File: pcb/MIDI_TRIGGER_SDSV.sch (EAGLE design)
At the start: 20 parts, among them IC1 AT90S2313P, IC7 7805TV, J1 DCJ0202

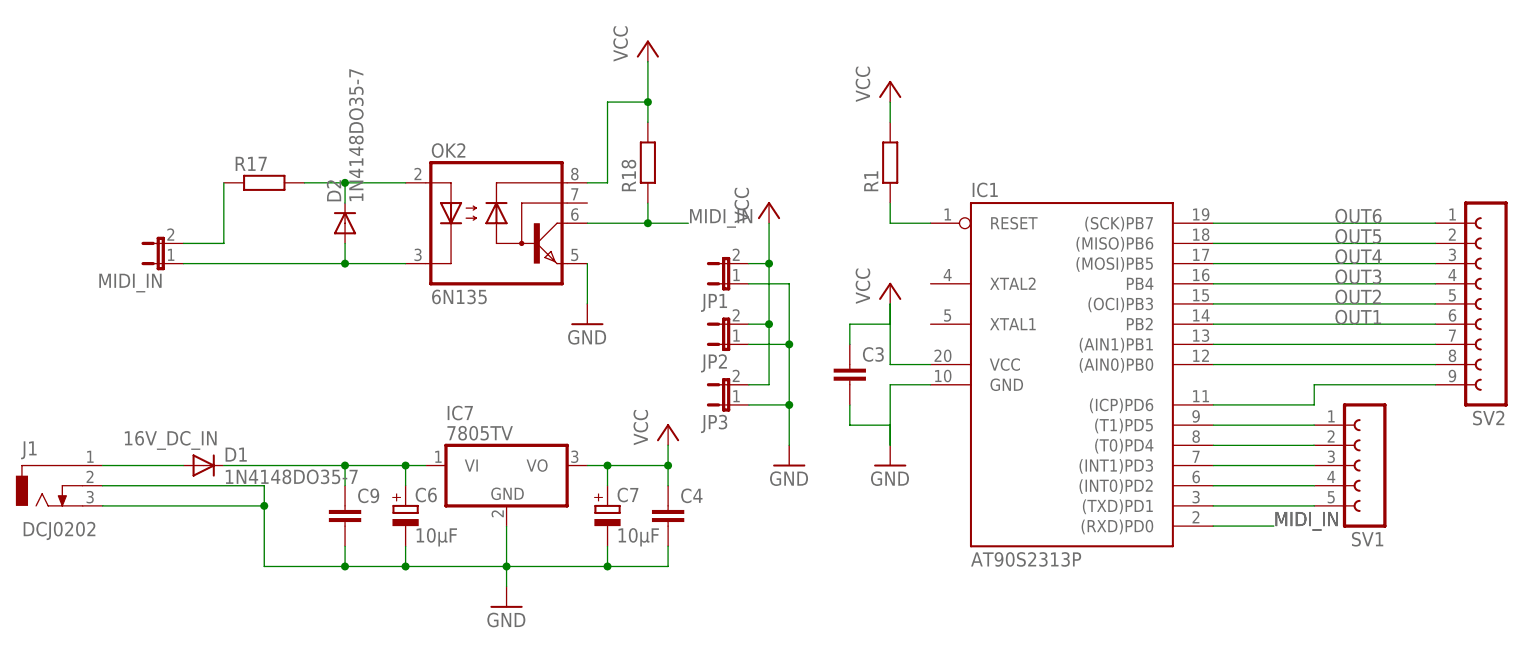
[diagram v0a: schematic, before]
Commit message: updated schematic and added picture of schematic for non-eagle users
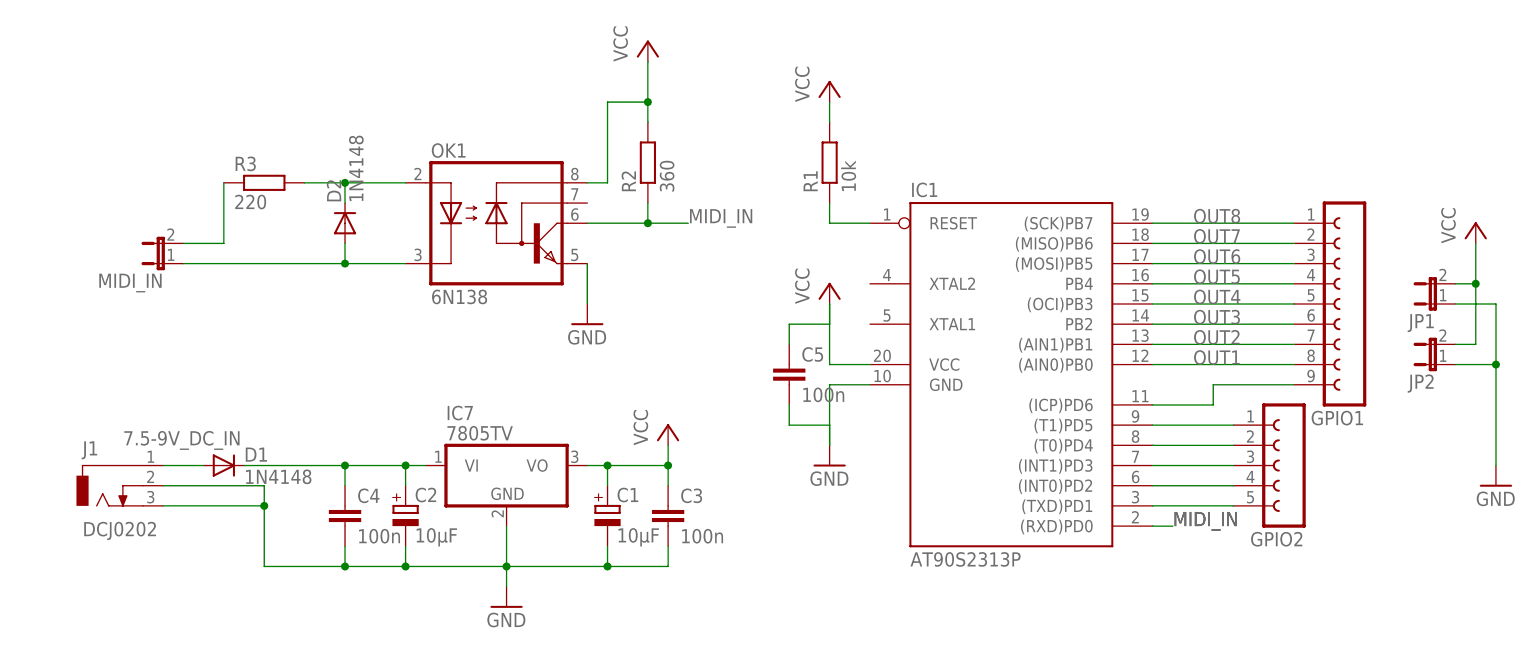
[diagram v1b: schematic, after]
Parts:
- removed C9: (no value), rcl:C-EU050-025X075
- removed JP3: (no value), jumper:JP1E
- removed SV1: (no value), con-lsta:FE05-1
- removed SV2: (no value), con-lsta:FE09-1
- added C5: 100n, rcl:C-EU050-025X075
- added GPIO1: (no value), con-lsta:FE09-1
- added GPIO2: (no value), con-lsta:FE05-1
- C3, C4: value (none) -> 100n
- D1, D2: value 1N4148DO35-7 -> 1N4148
- OK1: value 6N135 -> 6N138
- R1: value (none) -> 10k
- R2: value (none) -> 360
- R3: value (none) -> 220
- renumbered C6 to C2, C7 to C1, OK2 to OK1, R17 to R3, R18 to R2
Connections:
- net 16V_DC_IN renamed 7.5-9V_DC_IN
- removed net N$8: IC1.(AIN1)PB1, SV2.7
- removed net N$9: IC1.(AIN0)PB0, SV2.8
- new net OUT7: GPIO1.2, IC1.(MISO)PB6
- new net OUT8: GPIO1.1, IC1.(SCK)PB7
- net GND: now also C5.2; no longer C9.2, JP3.1
- net N$1: now also GPIO1.9; no longer SV2.9
- net N$2: now also GPIO2.1; no longer SV1.1
- net N$3: now also GPIO2.2; no longer SV1.2
- net N$4: now also C4.1; no longer C9.1
- net N$5: now also GPIO2.3; no longer SV1.3
- net N$6: now also GPIO2.4; no longer SV1.4
- net N$7: now also GPIO2.5; no longer SV1.5
- net OUT1: now also GPIO1.8, IC1.(AIN0)PB0; no longer IC1.PB2, SV2.6
- net OUT2: now also GPIO1.7, IC1.(AIN1)PB1; no longer IC1.(OCI)PB3, SV2.5
- net OUT3: now also GPIO1.6, IC1.PB2; no longer IC1.PB4, SV2.4
- net OUT4: now also GPIO1.5, IC1.(OCI)PB3; no longer IC1.(MOSI)PB5, SV2.3
- net OUT5: now also GPIO1.4, IC1.PB4; no longer IC1.(MISO)PB6, SV2.2
- net OUT6: now also GPIO1.3, IC1.(MOSI)PB5; no longer IC1.(SCK)PB7, SV2.1
- net VCC: now also C5.1; no longer C4.1, JP3.2
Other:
- moved on the sheet: C3, C4, D1, IC1, J1, JP1, JP2, R1
